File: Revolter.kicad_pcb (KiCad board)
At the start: 4 copper layers, 100 x 89 mm, 157 parts, among them IC1 LM5017, IC2 AP65111, IC3 INA181A1, IC4 INA181A1, IC5 INA181A1, J1 IO, J2 USB_A, P2 CAN, P3 IN+, P4 IN-, P5 MOTOR3, P6 MOTOR2, P7 MOTOR1, P8 SWD, P9 Motor, Q1 FDMT800100DC, Q2 FDMT800100DC, Q3 FDMT800100DC, Q4 FDMT800100DC, Q5 FDMT800100DC, Q6 FDMT800100DC, U1 STM32F40X_LQFP64, U2 IRS2186, U3 IRS2186, U4 IRS2186, U5 PCA82C251, U6 7805_SO8, Y1 Crystal

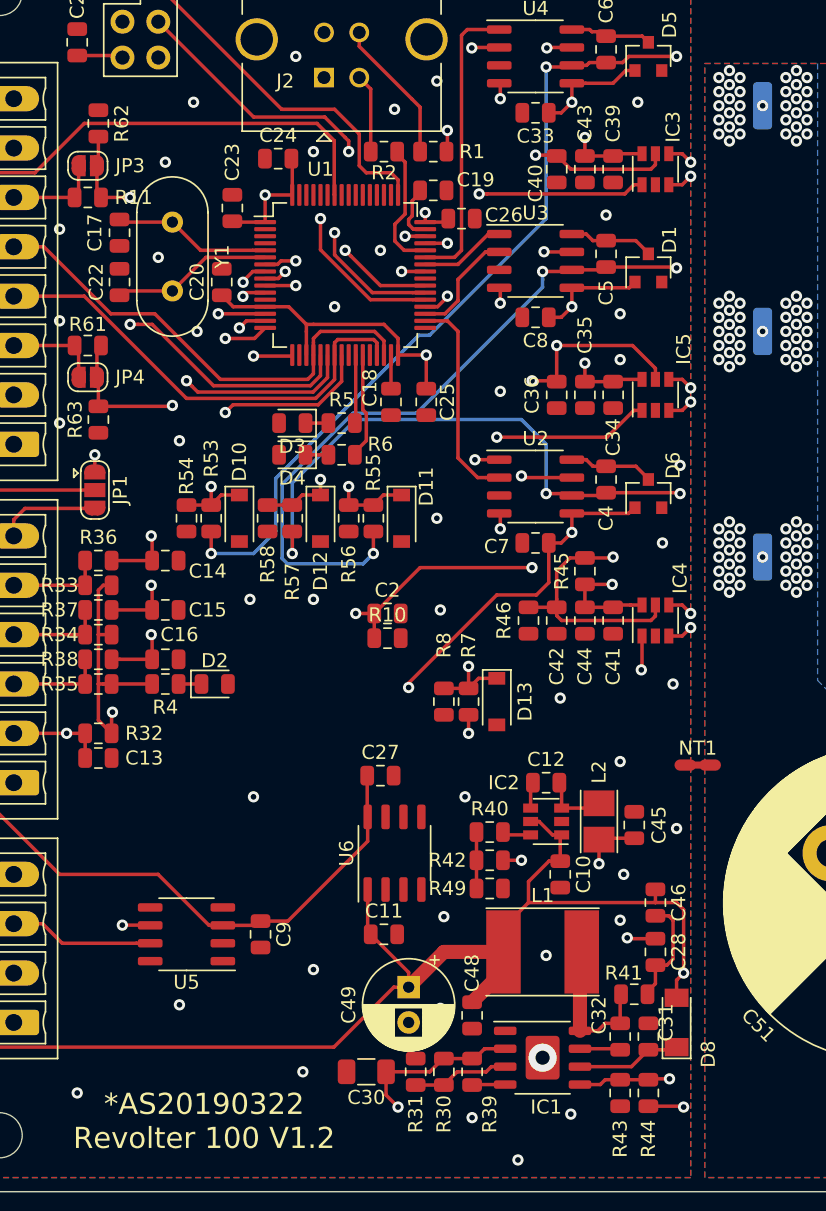
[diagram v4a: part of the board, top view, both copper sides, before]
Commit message: - fixed some issues with planes - moved some silkscreen labels - updated version/date label
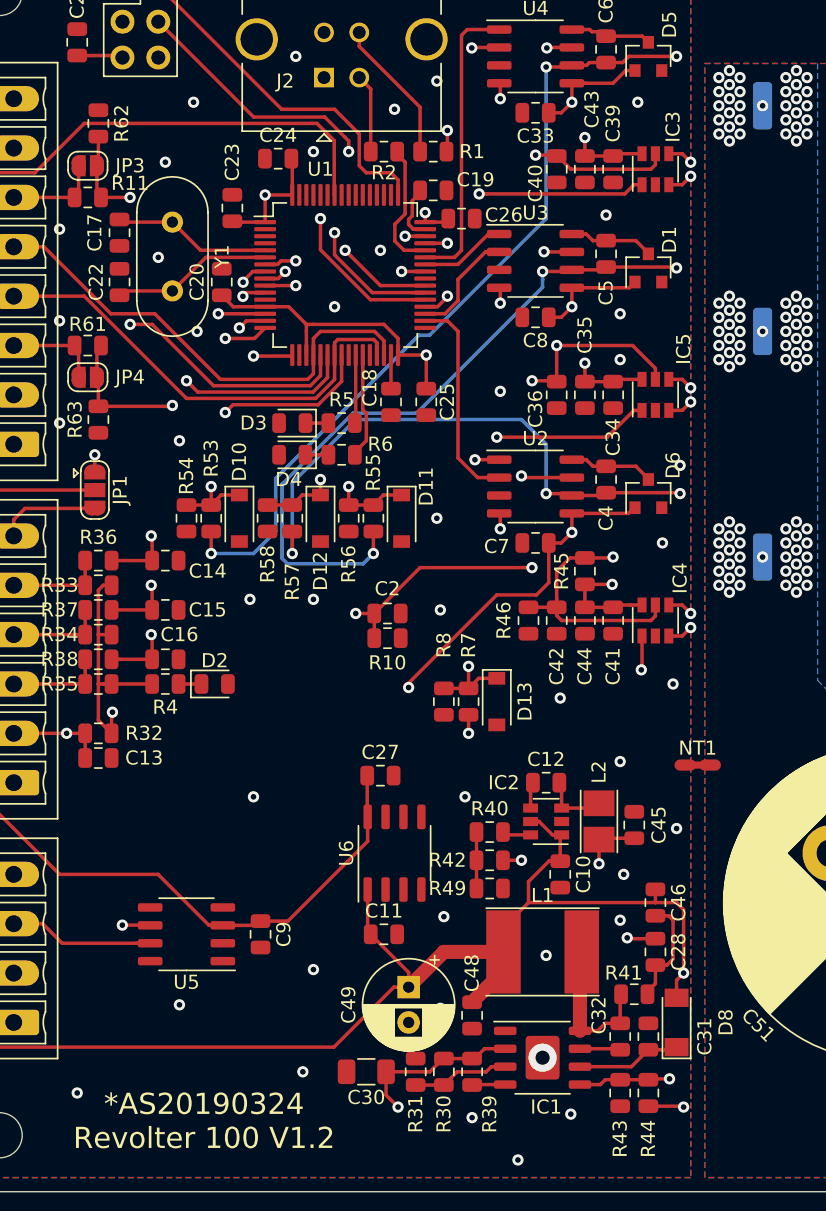
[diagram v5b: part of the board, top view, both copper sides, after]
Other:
- board text added: "*AS20190324 Revolter 100 V1.2"
- board text removed: "*AS20190322 Revolter 100 V1.2"
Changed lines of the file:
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@@
-(kicad_pcb (version 20171130) (host pcbnew "(5.0.0)")
+(kicad_pcb (version 20171130) (host pcbnew "(5.0.2)-1")
   (general
     (thickness 1.6)
@@
   )
   (setup
-    (last_trace_width 0.25)
+    (last_trace_width 0.8)
     (user_trace_width 0.8)
     (user_trace_width 1)
@@
     (pad_drill 3.2)
     (pad_to_mask_clearance 0.1)
+    (solder_mask_min_width 0.25)
     (aux_axis_origin 68 48)
     (visible_elements 7EFFF7FF)
@@
     (tags capacitor)
     (attr smd)
-    (fp_text reference C31 (at 1 1.25 90) (layer F.SilkS)
+    (fp_text reference C31 (at 0 4 90) (layer F.SilkS)
       (effects (font (size 1 1) (thickness 0.15)))
     )
@@
     (tags capacitor)
     (attr smd)
-    (fp_text reference C43 (at -3.25 0 270) (layer F.SilkS)
+    (fp_text reference C43 (at -4.25 -0.5 270) (layer F.SilkS)
       (effects (font (size 1 1) (thickness 0.15)))
     )
@@
     (tags capacitor)
     (attr smd)
-    (fp_text reference C36 (at 0 1.75 270) (layer F.SilkS)
+    (fp_text reference C36 (at 1 1.5 270) (layer F.SilkS)
       (effects (font (size 1 1) (thickness 0.15)))
     )
@@
     (tags capacitor)
     (attr smd)
-    (fp_text reference C2 (at 0 -1.65) (layer F.SilkS)
+    (fp_text reference C2 (at 0 -1.75) (layer F.SilkS)
       (effects (font (size 1 1) (thickness 0.15)))
     )
@@
     (tags "Diode Mini-MELF")
     (attr smd)
-    (fp_text reference D8 (at -2.25 2.25 90) (layer F.SilkS)
+    (fp_text reference D8 (at 0 3.5 90) (layer F.SilkS)
       (effects (font (size 1 1) (thickness 0.15)))
     )
@@
     (tags diode)
     (attr smd)
-    (fp_text reference D3 (at 0 -1.65 180) (layer F.SilkS)
+    (fp_text reference D3 (at 2.75 0 180) (layer F.SilkS)
       (effects (font (size 1 1) (thickness 0.15)))
     )
@@
     (tags diode)
     (attr smd)
-    (fp_text reference D4 (at 0 -1.65 180) (layer F.SilkS)
+    (fp_text reference D4 (at 0.25 -1.75 180) (layer F.SilkS)
       (effects (font (size 1 1) (thickness 0.15)))
     )
@@
     (tags resistor)
     (attr smd)
-    (fp_text reference R10 (at 0 -1.65) (layer F.SilkS)
+    (fp_text reference R10 (at 0 1.75) (layer F.SilkS)
       (effects (font (size 1 1) (thickness 0.15)))
     )
@@
     (tags resistor)
     (attr smd)
-    (fp_text reference R11 (at -3.25 0 180) (layer F.SilkS)
+    (fp_text reference R11 (at -3 1 180) (layer F.SilkS)
       (effects (font (size 1 1) (thickness 0.15)))
     )
@@
     (tags resistor)
     (attr smd)
-    (fp_text reference R47 (at 0 2.62) (layer B.SilkS)
+    (fp_text reference R47 (at 0 3.75) (layer B.SilkS)
       (effects (font (size 1 1) (thickness 0.15)) (justify mirror))
     )
@@
     (tags resistor)
     (attr smd)
-    (fp_text reference R3 (at 0 2.62) (layer B.SilkS)
+    (fp_text reference R3 (at 0 3.75) (layer B.SilkS)
       (effects (font (size 1 1) (thickness 0.15)) (justify mirror))
     )
@@
     )
   )
-  (gr_text "*AS20190322\nRevolter 100 V1.2" (at 86.5 132) (layer F.SilkS)
+  (gr_text "*AS20190324\nRevolter 100 V1.2" (at 86.5 132) (layer F.SilkS)
     (effects (font (size 1.5 1.5) (thickness 0.3)))
   )
@@
   )
   (zone (net 1) (net_name GNDPWR) (layer B.Cu) (hatch edge 0.508)
-    (connect_pads (clearance 0.25))
+    (connect_pads (clearance 0.5))
     (min_thickness 0.25)
     (fill yes (arc_segments 32) (thermal_gap 0.25) (thermal_bridge_width 1))
@@
   )
   (zone (net 1) (net_name GNDPWR) (layer F.Cu) (hatch edge 0.508)
-    (connect_pads (clearance 0.25))
+    (connect_pads (clearance 0.5))
     (min_thickness 0.25)
     (fill yes (arc_segments 32) (thermal_gap 0.25) (thermal_bridge_width 1))
@@
   )
   (zone (net 8) (net_name +BATT) (layer Power) (hatch edge 0.508)
-    (connect_pads (clearance 0.5))
+    (connect_pads (clearance 0.25))
     (min_thickness 0.25)
     (fill yes (arc_segments 32) (thermal_gap 0.25) (thermal_bridge_width 1))

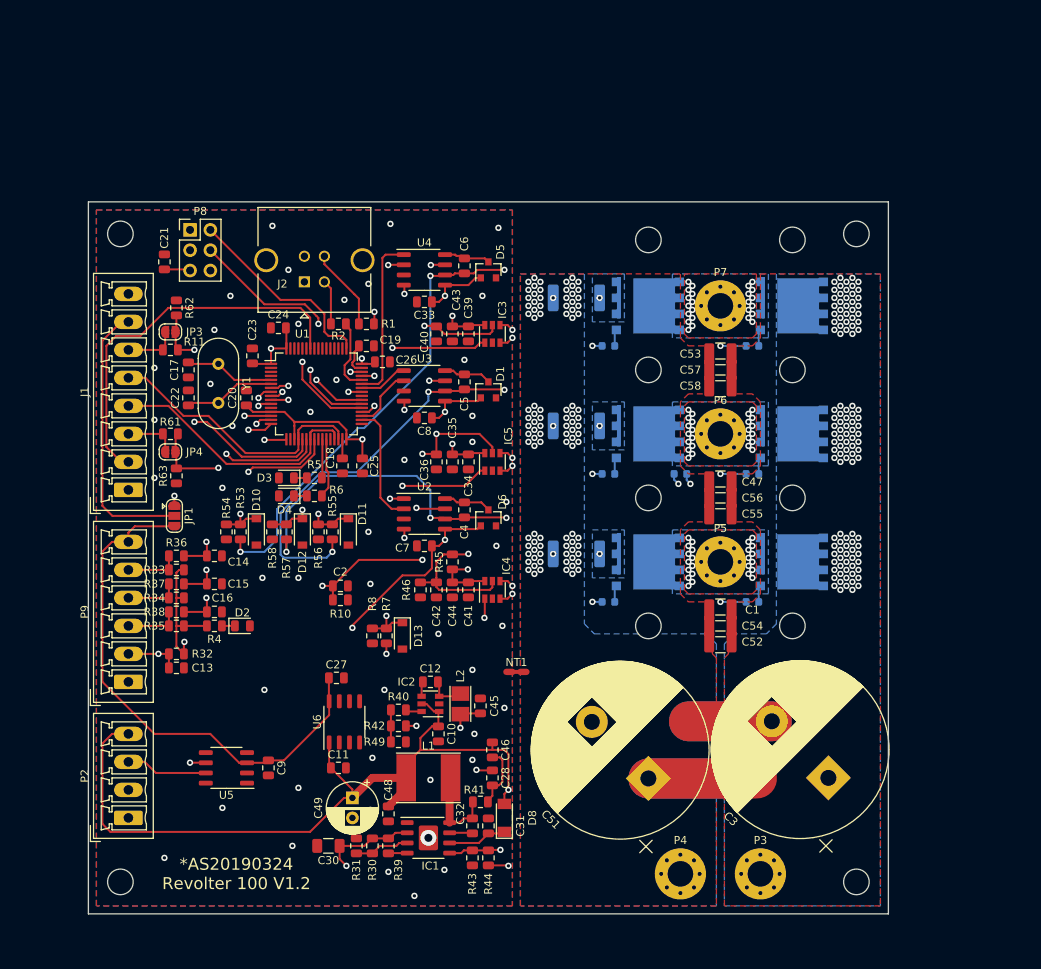
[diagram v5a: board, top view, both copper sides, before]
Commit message: - fixed ACS730 pin issue - added power supplies - added footprint library - added footprint for IRSM005
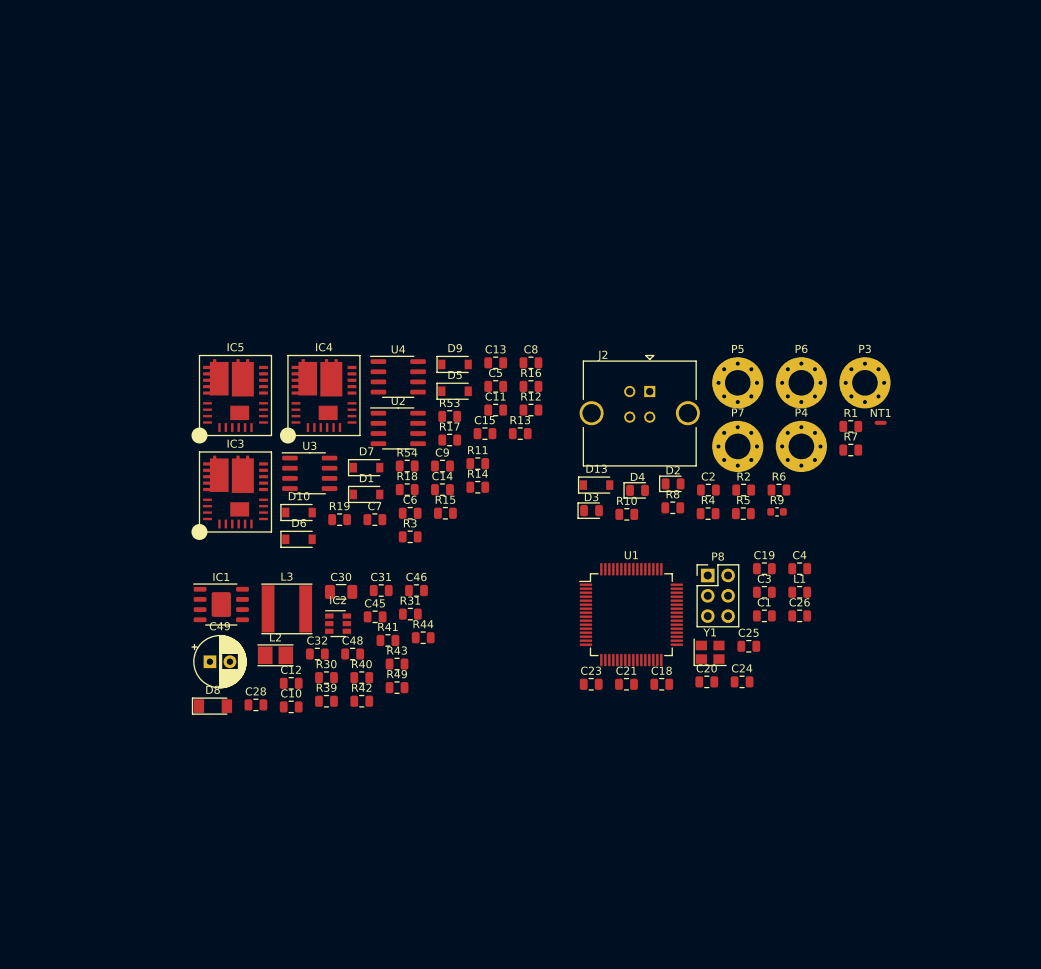
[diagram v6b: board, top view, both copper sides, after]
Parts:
- removed C16: 4n7, Capacitor_SMD:C_0805_2012Metric
- removed C17, C22: 15p, Capacitor_SMD:C_0805_2012Metric
- removed C27, C36, C40, C42: 100n, Capacitor_SMD:C_0805_2012Metric
- removed C33, C35, C43, C44: 1u, Capacitor_SMD:C_0805_2012Metric
- removed C34, C39, C41: 10n, Capacitor_SMD:C_0805_2012Metric
- removed C47, C52, C53, C54, C55, C56, C57, C58: 2u2 250V, Capacitor_SMD:C_1210_3225Metric
- removed C51: 1mF 100V, Capacitor_THT:CP_Radial_D22.0mm_P10.00mm_SnapIn
- removed D11, D12: 3V3, Diode_SMD:D_SOD-123
- removed J1: IO, Connector_Phoenix_MC:PhoenixContact_MCV_1,5_8-G-3.5_1x08_P3.50mm_Vertical
- removed JP1: Jumper_NC_Dual, Jumper:SolderJumper-3_P1.3mm_Open_RoundedPad1.0x1.5mm
- removed JP3, JP4: opt., Jumper:SolderJumper-2_P1.3mm_Open_RoundedPad1.0x1.5mm
- removed P2: CAN, Connector_Phoenix_MC:PhoenixContact_MCV_1,5_4-G-3.5_1x04_P3.50mm_Vertical
- removed P9: Motor, Connector_Phoenix_MC:PhoenixContact_MCV_1,5_6-G-3.5_1x06_P3.50mm_Vertical
- removed Q1, Q2, Q3, Q4, Q5, Q6: FDMT800100DC, Package_TO_SOT_SMD:PQFN_8x8
- removed R22, R23, R28, R29: 1R, Resistor_SMD:R_0603_1608Metric
- removed R32, R36, R37, R38, R45, R46: 10k, Resistor_SMD:R_0805_2012Metric
- removed R33, R34, R35: 2k2, Resistor_SMD:R_0805_2012Metric
- removed R47, R48: WSLF2512L5000FEB, Resistor_SMD:R_2512_6332Metric
- removed R55, R57: 100k, Resistor_SMD:R_0805_2012Metric
- removed R56, R58: 3k3, Resistor_SMD:R_0805_2012Metric
- removed R61: 1k, Resistor_SMD:R_0805_2012Metric
- removed R62, R63: 1k5, Resistor_SMD:R_0805_2012Metric
- removed REF** (x12): MountingHole_3.2mm_M3, MountingHole:MountingHole_3.2mm_M3
- removed U5: PCA82C251, Package_SO:SO-8_3.9x4.9mm_P1.27mm
- removed U6: 7805_SO8, Package_SO:SO-8_3.9x4.9mm_P1.27mm
- added D7: D, Diode_SMD:D_SOD-123, F.Cu at (102.8, 81.2)
- added D9: 3V3, Diode_SMD:D_SOD-123, F.Cu at (113.8, 68.3)
- added L3: VLS6045EX-221M, Inductor_SMD:L_Taiyo-Yuden_NR-60xx, F.Cu at (92.8, 98.9)
- added R12: 1R, Resistor_SMD:R_0805_2012Metric, F.Cu at (123.3, 74.0)
- added R13: 1R, Resistor_SMD:R_0805_2012Metric, F.Cu at (122.0, 77.0)
- added R14: 100k, Resistor_SMD:R_0805_2012Metric, F.Cu at (116.7, 83.7)
- added R15: 3k3, Resistor_SMD:R_0805_2012Metric, F.Cu at (112.6, 86.9)
- added R18: 100k, Resistor_SMD:R_0805_2012Metric, F.Cu at (107.8, 84.0)
- added R19: 3k3, Resistor_SMD:R_0805_2012Metric, F.Cu at (99.4, 87.7)
- C1: value 2u2 250V -> 15p; footprint Capacitor_SMD:C_1210_3225Metric -> Capacitor_SMD:C_0805_2012Metric
- C11, C9: value 100n -> 1u
- C13, C15: value 4n7 -> 1u
- C14: value 4n7 -> 1n
- C3: value 1mF 100V -> 15p; footprint Capacitor_THT:CP_Radial_D22.0mm_P10.00mm_SnapIn -> Capacitor_SMD:C_0805_2012Metric
- C7, C8: value 1u -> 1n
- D1, D5: value BAS21L -> D; footprint Diode_SMD:D_SOT-23_ANK -> Diode_SMD:D_SOD-123
- D2: value LED -> BLUE
- D6: value BAS21L -> 3V3; footprint Diode_SMD:D_SOT-23_ANK -> Diode_SMD:D_SOD-123
- IC3, IC4, IC5: value INA181A1 -> IRSM005; footprint Package_TO_SOT_SMD:SOT-23-6 -> Revolter_100V:IRSM005
- L1: value VLS6045EX-221M -> 100u; footprint Inductor_SMD:L_Taiyo-Yuden_NR-60xx_HandSoldering -> Inductor_SMD:L_0805_2012Metric
- R11: value 1k -> 1R
- R16, R17: footprint Resistor_SMD:R_0603_1608Metric -> Resistor_SMD:R_0805_2012Metric; moved to F.Cu
- R3: value WSLF2512L5000FEB -> 1R; footprint Resistor_SMD:R_2512_6332Metric -> Resistor_SMD:R_0805_2012Metric; moved to F.Cu
- R4: value 2k2 -> 470R
- R9: moved to F.Cu
- U1: value STM32F40X_LQFP64 -> STM32F405RGTx
- U2, U3, U4: value IRS2186 -> ACS730xLCTR-50AB; footprint Package_SO:SO-8_3.9x4.9mm_P1.27mm -> Package_SO:SOIC-8_3.9x4.9mm_P1.27mm
- Y1: value Crystal -> 8MHz; footprint Crystal:Crystal_HC49-U_Vertical -> Crystal:Crystal_SMD_3225-4Pin_3.2x2.5mm
- moved C21 78.3 mm to (135.3, 108.3), turned to 0 degrees
- moved P8 77.8 mm to (145.4, 94.7)
- moved C24 72.9 mm to (149.7, 108.0)
- moved Y1 71.3 mm to (145.7, 104.3), turned to 0 degrees
- moved C20 67.6 mm to (145.3, 108.0), turned to 0 degrees
- moved R4 63.3 mm to (145.5, 87.0), turned to 0 degrees
- moved P3 62.8 mm to (165.1, 70.6)
- moved R7 62.5 mm to (163.3, 79.0), turned to 0 degrees
- moved R1 61.9 mm to (163.3, 76.1), turned to 0 degrees
- moved C26 61.1 mm to (156.9, 99.8), turned to 0 degrees
- moved C23 59.0 mm to (130.8, 108.3), turned to 0 degrees
- moved R6 58.1 mm to (154.3, 84.0)
- moved C19 57.0 mm to (152.5, 93.8)
- moved D2 56.7 mm to (141.1, 83.2)
- moved P4 55.5 mm to (157.1, 78.6)
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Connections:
- C1 pad 1: +BATT -> GND
- C1 pad 2: GNDPWR -> Net-(C1-Pad2)
- C11 pad 1: +12V -> +3V3
- C13 pad 1: GND -> Net-(C13-Pad1)
- C13 pad 2: /Filters/TEMP_IN -> Net-(C13-Pad2)
- C14 pad 1: /Filters/HALL3_OUT -> Net-(C14-Pad1)
- C15 pad 1: /Filters/HALL2_OUT -> +3V3
- C18 pad 1: Net-(C18-Pad1) -> GND
- C18 pad 2: GND -> Net-(C18-Pad2)
- C20 pad 2: +3V3 -> Net-(C20-Pad2)
- C3 pad 1: +BATT -> Net-(C3-Pad1)
- C3 pad 2: GNDPWR -> GND
- C4 pad 1: Net-(C4-Pad1) -> GND
- C4 pad 2: /Mosfet driver/H1_VS -> +3V3
- C5 pad 2: /Mosfet driver/H2_VS -> Net-(C5-Pad2)
- C6 pad 2: /Mosfet driver/H3_VS -> Net-(C6-Pad2)
- C7 pad 1: +12V -> Net-(C7-Pad1)
- C8 pad 1: +12V -> Net-(C8-Pad1)
- C9 pad 1: +5V -> +3V3
- D1 pad 2: +12V -> Net-(D1-Pad2)
- D10 pad 1: /MCU/VOLTAGE_1 -> /MCU/VOLTAGE_V
- D5 pad 2: +12V -> Net-(D5-Pad2)
- D6 pad 1: Net-(C4-Pad1) -> /MCU/VOLTAGE_W
- D6 pad 2: +12V -> GND
- IC1 pad 7: Net-(C32-Pad1) -> Net-(C32-Pad2)
- IC1 pad 8: Net-(C32-Pad2) -> Net-(C32-Pad1)
- IC2 pad 3: Net-(C12-Pad2) -> Net-(C12-Pad1)
- IC2 pad 4: Net-(C12-Pad1) -> Net-(C12-Pad2)
- IC3 pad 1: /MCU/CURRENT_3 -> Net-(C5-Pad1)
- IC3 pad 2: GND -> Net-(D1-Pad2)
- IC3 pad 3: /Mosfet driver/H3_LOW -> GND
- IC3 pad 4: GNDPWR -> /MCU/HU
- IC3 pad 5: U/2 -> /MCU/LU
- IC3 pad 6: +3V3 -> GND
- IC4 pad 1: /MCU/CURRENT_1 -> Net-(C6-Pad1)
- IC4 pad 2: GND -> Net-(D5-Pad2)
- IC4 pad 3: /Mosfet driver/H1_LOW -> GND
- IC4 pad 4: GNDPWR -> /MCU/HW
- IC4 pad 5: U/2 -> /MCU/LW
- IC4 pad 6: +3V3 -> GND
- IC5 pad 1: /MCU/CURRENT_2 -> Net-(C13-Pad1)
- IC5 pad 2: GND -> Net-(D7-Pad2)
- IC5 pad 3: /Mosfet driver/H2_LOW -> GND
- IC5 pad 4: GNDPWR -> /MCU/HV
- IC5 pad 5: U/2 -> /MCU/LV
- IC5 pad 6: +3V3 -> GND
- L1 pad 1: +12V -> +3V3
- L1 pad 2: Net-(C32-Pad2) -> Net-(C20-Pad2)
- L2 pad 1: Net-(C12-Pad2) -> Net-(C12-Pad1)
- P5 pad 1: /Mosfet driver/H1_VS -> Net-(P5-Pad1)
- P6 pad 1: /Mosfet driver/H2_VS -> Net-(P6-Pad1)
- P7 pad 1: /Mosfet driver/H3_VS -> Net-(P7-Pad1)
- R11 pad 1: /MCU/SCK_ADC_EXT -> Net-(IC3-Pad9)
- R11 pad 2: Net-(J1-Pad6) -> Net-(IC3-Pad7)
- R16 pad 1: Net-(Q1-Pad1) -> Net-(IC5-Pad24)
- R16 pad 2: /Mosfet driver/M_H1 -> Net-(IC5-Pad25)
- R17 pad 1: Net-(Q2-Pad1) -> Net-(IC5-Pad9)
- R17 pad 2: /Mosfet driver/M_L1 -> Net-(IC5-Pad7)
- R3 pad 1: GNDPWR -> Net-(IC3-Pad24)
- R3 pad 2: /Mosfet driver/H2_LOW -> Net-(IC3-Pad25)
- R39 pad 1: Net-(IC1-Pad4) -> +BATT
- R39 pad 2: +BATT -> Net-(IC1-Pad4)
- R41 pad 2: Net-(C32-Pad2) -> Net-(C32-Pad1)
- R53 pad 1: /Mosfet driver/H3_VS -> /MCU/VOLTAGE_V
- R53 pad 2: /MCU/VOLTAGE_1 -> /Mosfet driver/Phase_U
- R54 pad 1: GND -> /MCU/VOLTAGE_V
- R54 pad 2: /MCU/VOLTAGE_1 -> GND
- U1 pad 10: /MCU/CURRENT_3 -> /MCU/CURRENT_W
- U1 pad 13: +3V3 -> Net-(C20-Pad2)
- U1 pad 14: /MCU/VOLTAGE_1 -> /MCU/VOLTAGE_U
- U1 pad 15: /MCU/VOLTAGE_2 -> /MCU/VOLTAGE_V
- U1 pad 16: /MCU/VOLTAGE_3 -> /MCU/VOLTAGE_W
- U1 pad 24: /Filters/TEMP_IN -> /MCU/TEMP_MOTOR
- U1 pad 29: /MCU/TX_SCL_MOSI -> Net-(U1-Pad29)
- U1 pad 30: /MCU/RX_SDA_NSS -> Net-(U1-Pad30)
- U1 pad 31: Net-(C18-Pad1) -> Net-(C18-Pad2)
- U1 pad 34: /MCU/L1 -> /MCU/LU
- U1 pad 35: /MCU/L2 -> /MCU/LV
- U1 pad 36: /MCU/L3 -> /MCU/LW
- U1 pad 37: /Filters/HALL1_OUT -> /MCU/HALL_U
- U1 pad 38: /Filters/HALL2_OUT -> /MCU/HALL_V
- U1 pad 39: /Filters/HALL3_OUT -> /MCU/HALL_W
- U1 pad 41: /MCU/H1 -> /MCU/HU
- U1 pad 42: /MCU/H2 -> /MCU/HV
- U1 pad 43: /MCU/H3 -> /MCU/HW
- U1 pad 5: Net-(C17-Pad1) -> Net-(C3-Pad1)
- U1 pad 58: /MCU/SERVO -> Net-(U1-Pad58)
- U1 pad 6: Net-(C22-Pad1) -> Net-(C1-Pad2)
- U1 pad 61: /CAN bus transceiver/CAN_RX -> /MCU/CAN_RX
- U1 pad 62: /CAN bus transceiver/CAN_TX -> /MCU/CAN_TX
- U1 pad 8: /MCU/CURRENT_1 -> /MCU/CURRENT_U
- U1 pad 9: /MCU/CURRENT_2 -> /MCU/CURRENT_V
- U2 pad 1: /MCU/H1 -> /Mosfet driver/Phase_U
- U2 pad 2: /MCU/L1 -> /Mosfet driver/Phase_U
- U2 pad 3: GND -> Net-(IC3-Pad10)
- U2 pad 4: /Mosfet driver/M_L1 -> Net-(IC3-Pad10)
- U2 pad 5: +12V -> GND
- U2 pad 6: /Mosfet driver/H1_VS -> Net-(C7-Pad1)
- U2 pad 7: /Mosfet driver/M_H1 -> /MCU/CURRENT_U
- U2 pad 8: Net-(C4-Pad1) -> +3V3
- U3 pad 1: /MCU/H2 -> /Mosfet driver/Phase_W
- U3 pad 2: /MCU/L2 -> /Mosfet driver/Phase_W
- U3 pad 3: GND -> Net-(IC4-Pad10)
- U3 pad 4: /Mosfet driver/M_L2 -> Net-(IC4-Pad10)
- U3 pad 5: +12V -> GND
- U3 pad 6: /Mosfet driver/H2_VS -> Net-(C8-Pad1)
- U3 pad 7: /Mosfet driver/M_H2 -> /MCU/CURRENT_W
- U3 pad 8: Net-(C5-Pad1) -> +3V3
- U4 pad 1: /MCU/H3 -> /Mosfet driver/Phase_V
- U4 pad 2: /MCU/L3 -> /Mosfet driver/Phase_V
- U4 pad 3: GND -> Net-(IC5-Pad10)
- U4 pad 4: /Mosfet driver/M_L3 -> Net-(IC5-Pad10)
- U4 pad 5: +12V -> GND
- U4 pad 6: /Mosfet driver/H3_VS -> Net-(C14-Pad1)
- U4 pad 7: /Mosfet driver/M_H3 -> /MCU/CURRENT_V
- U4 pad 8: Net-(C6-Pad1) -> +3V3
- Y1 pad 1: Net-(C17-Pad1) -> Net-(C1-Pad2)
- Y1 pad 2: Net-(C22-Pad1) -> GND
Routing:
- net +12V: track 232.7 -> 0.00 mm, vias 6 -> 0
- net +BATT: track 128.2 -> 0.00 mm, vias 113 -> 0
- net +3V3: track 103.7 -> 0.00 mm, vias 12 -> 0
- net /MCU/ADC_TEMP: track 88.0 -> 0.00 mm, vias 4 -> 0
- net /Mosfet driver/H3_VS: track 86.5 -> 0.00 mm, vias 27 -> 0
- net /Mosfet driver/H2_VS: track 78.1 -> 0.00 mm, vias 27 -> 0
- net U/2: track 70.9 -> 0.00 mm, vias 4 -> 0
- net +5V: track 67.0 -> 0.00 mm
- net /Mosfet driver/H1_VS: track 65.3 -> 0.00 mm, vias 27 -> 0
- net /Mosfet driver/M_H1: track 57.9 -> 0.00 mm, vias 2 -> 0
- net /Mosfet driver/M_H2: track 57.4 -> 0.00 mm, vias 2 -> 0
- net /Mosfet driver/M_H3: track 56.3 -> 0.00 mm, vias 2 -> 0
- net /Filters/HALL1_OUT: track 53.2 -> 0.00 mm, vias 2 -> 0
- net GNDPWR: track 52.2 -> 0.00 mm, vias 102 -> 0
- net /MCU/SERVO: track 48.0 -> 0.00 mm
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- removed copper zone on Power, net +3V3
- removed copper zone on B.Cu, net +BATT
- removed copper zone on F.Cu, net +BATT
- removed copper zone on Power, net +BATT
- removed copper zone on B.Cu, net /Mosfet driver/H1_LOW
- removed copper zone on B.Cu, net /Mosfet driver/H1_VS
- removed copper zone on F.Cu, net /Mosfet driver/H1_VS
- removed copper zone on Power, net /Mosfet driver/H1_VS
- removed copper zone on Sig, net /Mosfet driver/H1_VS
- removed copper zone on B.Cu, net /Mosfet driver/H2_LOW
- removed copper zone on B.Cu, net /Mosfet driver/H2_VS
- removed copper zone on F.Cu, net /Mosfet driver/H2_VS
- removed copper zone on Power, net /Mosfet driver/H2_VS
- removed copper zone on Sig, net /Mosfet driver/H2_VS
- removed copper zone on B.Cu, net /Mosfet driver/H3_LOW
- removed copper zone on B.Cu, net /Mosfet driver/H3_VS
- removed copper zone on F.Cu, net /Mosfet driver/H3_VS
- removed copper zone on Power, net /Mosfet driver/H3_VS
- removed copper zone on Sig, net /Mosfet driver/H3_VS
- removed copper zone on B.Cu, net GND
- removed copper zone on F.Cu, net GND
- removed copper zone on B.Cu, net GNDPWR
- removed copper zone on F.Cu, net GNDPWR
- removed copper zone on Power, net GNDPWR
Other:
- board outline removed
- board text removed: "*AS20190324 Revolter 100 V1.2"
- board text removed: "+ H L -"
- board text removed: "+ H3 H2 H1 T -"
- board text removed: "- + A1 CC REV A2 PPM -"
